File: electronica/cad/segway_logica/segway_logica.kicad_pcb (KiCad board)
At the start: 2 copper layers, 100 x 82 mm, 17 parts, among them J20 Cable lógica-potencia 2x8, J4 Paro MPT0,5 1=GND 2=PARO (NC), J7 Encoder IZQ PT1,5 1=V 2=A 3=B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, J8 Encoder DER PT1,5 1=GND 2=A 3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

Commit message: electronica: PCB v0.1 de la placa de potencia, una cara, DRC limpio (ELE-032)
- Placa de potencia 150 x 110 mm: barra VM_BUS, lomo GND en estrella entre los
  pads de los fusibles, ramas por canal de motor, franja de servos y banda
  lógica. DRC 0 errores, 0 sin conectar, 0 de paridad; 7 puentes fijos.
- Ruteo híbrido (TEC-05): esqueleto y bus I2C a mano (J20 -> A7 -> A5 ->
  corredor bajo los módulos -> A6), Freerouting solo para nets simples, vías
  prohibidas sobre componentes y poda automática de puentes redundantes.
- Cable J20 y GPIO reordenados por geometría (VBAT en GPIO3, ALERT en GPIO8,
  columna par servos/IN); placa de lógica regenerada y re-verificada (0/0/0).
- J20.11 sin conexión en la potencia; INA226 sin separador opcional.
- Supuestos SUP-04/15/24/28/72 actualizados y SUP-75 a SUP-77 nuevos.

Co-Authored-By: Claude Opus 5.5 <noreply@anthropic.com>
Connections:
- A1 pad 12: /VBAT_ADC -> /INA_ALERT
- A1 pad 13: /INA_ALERT -> /VBAT_ADC
- A1 pad 15: /IN1_DER_MCU -> /SERVO_IZQ_MCU
- A1 pad 16: /IN2_DER_MCU -> /SERVO_DER_MCU
- A1 pad 17: /IN1_IZQ_MCU -> /IN2_DER_MCU
- A1 pad 18: /IN2_IZQ_MCU -> /IN1_DER_MCU
- A1 pad 19: /SERVO_IZQ_MCU -> /IN2_IZQ_MCU
- A1 pad 20: /SERVO_DER_MCU -> /IN1_IZQ_MCU
- J20 pad 1: /INA_ALERT -> /VBAT_ADC
- J20 pad 10: /SERVO_IZQ_MCU -> /IN2_IZQ_MCU
- J20 pad 12: /SERVO_DER_MCU -> /IN1_IZQ_MCU
- J20 pad 2: /IN1_DER_MCU -> /SERVO_IZQ_MCU
- J20 pad 3: /VBAT_ADC -> /INA_ALERT
- J20 pad 4: /IN2_DER_MCU -> /SERVO_DER_MCU
- J20 pad 6: /IN1_IZQ_MCU -> /IN2_DER_MCU
- J20 pad 8: /IN2_IZQ_MCU -> /IN1_DER_MCU
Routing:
- net /INA_ALERT: track 15.2 -> 25.4 mm
- net /VBAT_ADC: track 25.4 -> 15.2 mm

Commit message: electronica: expansión de la placa de lógica, tiras hembra junto a la ESP32-S3 (ELE-037)
Pedido del equipo: pines hembra en paralelo a la controladora para sumar
sensores (ultrasonido, infrarrojo).

- J24 y J25: tiras hembra 1x22 pegadas a cada hilera de A1, pin a pin.
  Huellas propias con el courtyard recortado del lado de A1.
- J26: tira hembra 1x6 de alimentación (GND, 3V3, 5V_MCU).
- J20.11 sin conexión también en la lógica; rótulos de cobre bajados
  para que el relleno GND no quede partido.
- generar_esquema.py: altura correcta de los conectores de una hilera
  (antes se pisaban las etiquetas y el comparador detectaba cortos).
- ERC 0, netlist coincidente, DRC 0 errores / 0 sin conectar / 0 paridad.
- SUP-72 y SUP-77 cambiados; SUP-78 y SUP-79 nuevos.

Co-Authored-By: Claude Opus 5.5 <noreply@anthropic.com>
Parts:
- added J24: Expansión ESP32 IZQ (A1.1-22), segway_modulos:Zocalo_expansion_izq_1x22_P2.54mm, F.Cu at (91.4, 41.9)
- added J25: Expansión ESP32 DER (A1.23-44), segway_modulos:Zocalo_expansion_der_1x22_P2.54mm, F.Cu at (121.9, 41.9)
- added J26: Alim. sensores 1-2 GND 3-4 3V3 5-6 5V, Connector_PinSocket_2.54mm:PinSocket_1x06_P2.54mm_Vertical, F.Cu at (63.5, 91.4)
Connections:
- A1 pad 14: unconnected-(A1-GPIO46-Pad14) -> /GPIO46
- A1 pad 24: unconnected-(A1-GPIO43/TX-Pad24) -> /GPIO43
- A1 pad 25: unconnected-(A1-GPIO44/RX-Pad25) -> /GPIO44
- A1 pad 26: unconnected-(A1-GPIO1-Pad26) -> /GPIO1
- A1 pad 27: unconnected-(A1-GPIO2-Pad27) -> /GPIO2
- A1 pad 28: unconnected-(A1-GPIO42-Pad28) -> /GPIO42
- A1 pad 29: unconnected-(A1-GPIO41-Pad29) -> /GPIO41
- A1 pad 3: unconnected-(A1-RST-Pad3) -> /RST
- A1 pad 30: unconnected-(A1-GPIO40-Pad30) -> /GPIO40
- A1 pad 31: unconnected-(A1-GPIO39-Pad31) -> /GPIO39
- A1 pad 32: unconnected-(A1-GPIO38-Pad32) -> /GPIO38
- A1 pad 33: unconnected-(A1-GPIO37-Pad33) -> /GPIO37
- A1 pad 34: unconnected-(A1-GPIO36-Pad34) -> /GPIO36
- A1 pad 35: unconnected-(A1-GPIO35-Pad35) -> /GPIO35
- A1 pad 36: unconnected-(A1-GPIO0-Pad36) -> /GPIO0
- A1 pad 37: unconnected-(A1-GPIO45-Pad37) -> /GPIO45
- A1 pad 38: unconnected-(A1-GPIO48-Pad38) -> /GPIO48
- A1 pad 39: unconnected-(A1-GPIO47-Pad39) -> /GPIO47
- A1 pad 40: unconnected-(A1-GPIO21-Pad40) -> /GPIO21
- A1 pad 41: unconnected-(A1-GPIO20-Pad41) -> /GPIO20
- A1 pad 42: unconnected-(A1-GPIO19-Pad42) -> /GPIO19
- J20 pad 11: /GND -> unconnected-(J20-Pin_11-Pad11)
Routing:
- net /5V_MCU: track 10.2 -> 20.8 mm
- net /3V3_MCU: track 168.1 -> 177.0 mm
- net /GND: track 34.9 -> 43.5 mm
- net /GPIO48: track 0.00 -> 2.54 mm
- net /GPIO47: track 0.00 -> 2.54 mm
- net /GPIO45: track 0.00 -> 2.54 mm
- net /GPIO44: track 0.00 -> 2.54 mm
- net /GPIO43: track 0.00 -> 2.54 mm
- net /GPIO42: track 0.00 -> 2.54 mm
- net /GPIO41: track 0.00 -> 2.54 mm
- net /GPIO40: track 0.00 -> 2.54 mm
- net /GPIO39: track 0.00 -> 2.54 mm
- net /GPIO38: track 0.00 -> 2.54 mm
- net /GPIO37: track 0.00 -> 2.54 mm
- net /GPIO36: track 0.00 -> 2.54 mm
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
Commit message: electronica: rótulos de cobre, revisión independiente y control eléctrico (ELE-039)
- Rótulos de polaridad y de fusibles en el cobre de las dos placas,
  ubicados con ubicar_rotulos.py sin partir el relleno GND (SUP-14).
- Revisión independiente del conexionado contra las fichas: módulos,
  cable, polaridades y niveles correctos. Riesgos nuevos: A7 y A8 entran
  girados y queman (SUP-80), aleta de Q1 con tensión (SUP-20), I2C junto
  a PWM en el cable (SUP-81).
- auditoria_electrica.py: control repetible del sistema (cable, pines
  críticos, 5 V lejos de la ESP32, módulos girados, I2C, cuellos de
  pista, niveles). Informe: 0 fallas, 6 avisos.
- J26 reordenado con GND en el medio; textos de la Blue Pill en la
  especificación corregidos.
- ERC 0 y netlist coincidente; DRC 0/0/0 en las dos placas; salidas de
  fabricación regeneradas.

Co-Authored-By: Claude Opus 5.5 <noreply@anthropic.com>
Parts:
- J26: value Alim. sensores 1-2 GND 3-4 3V3 5-6 5V -> Alim. sensores 1-2 3V3 3-4 GND 5-6 5V
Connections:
- J26 pad 1: /GND -> /3V3_MCU
- J26 pad 2: /GND -> /3V3_MCU
- J26 pad 3: /3V3_MCU -> /GND
- J26 pad 4: /3V3_MCU -> /GND
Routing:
- net /GND: track 43.5 -> 38.1 mm
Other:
- board text added: "1"
- board text added: "ENC IZQ"
- board text added: "G"

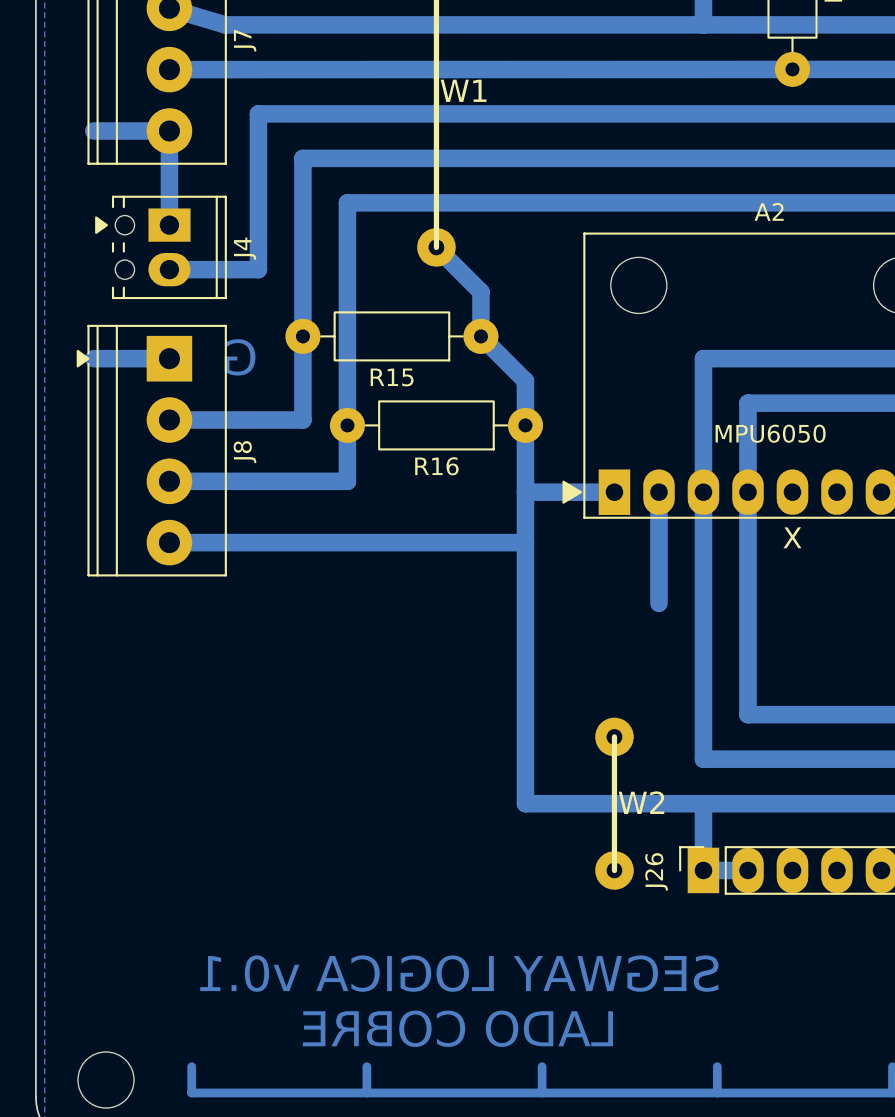
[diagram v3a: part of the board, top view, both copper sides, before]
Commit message: electronica: PCB v0.2 de las dos placas, auditada (ELE-040)
- J3 y J4 pasan a pads para soldar el cable del interruptor y del paro.
- Montaje: A1-A4 en zócalo, A5-A8 soldados (DEC-20). A1 codificada:
  pin 24 cortado y posición tapada (revisión independiente: entraba
  girada o corrida y se quemaba).
- auditoria_electrica.py prueba giros y corrimientos de los módulos
  enchufados; 0 fallas, 3 avisos.
- Rótulos ambiguos de fusibles y VCC quitados; continuidad del cable
  J20 antes de enchufar; precinto en J3.
- Documentación v0.2, lista de compras, fabricación en rev-0.2.
- ERC 0, netlist coincidente, DRC 0/0/0 en las dos placas.

Co-Authored-By: Claude Opus 5.5 <noreply@anthropic.com>
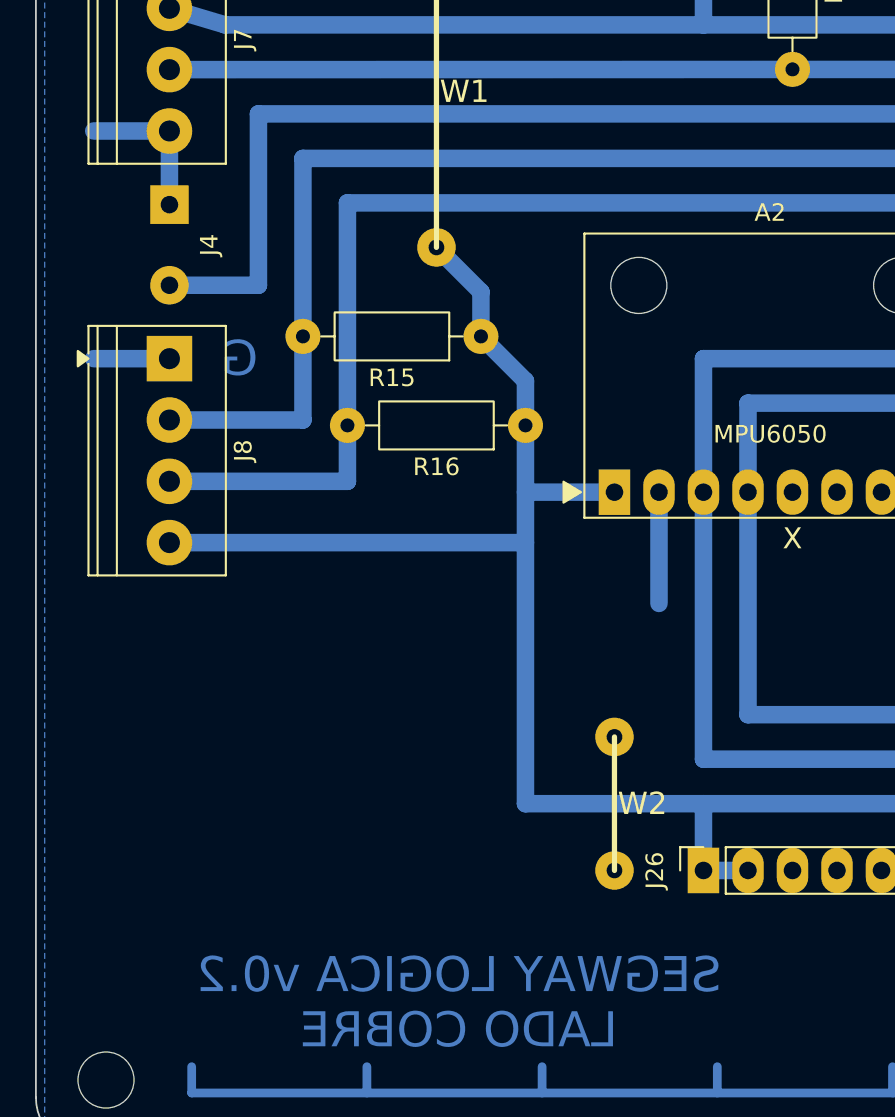
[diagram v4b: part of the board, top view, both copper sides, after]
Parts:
- J4: value Paro MPT0,5 1=GND 2=PARO (NC) -> Paro NC 1=GND 2=PARO, cable soldado; footprint TerminalBlock_Phoenix:TerminalBlock_Phoenix_MPT-0,5-2-2.54_1x02_P2.54mm_Horizontal -> Connector_Wire:SolderWire-0.5sqmm_1x02_P4.6mm_D0.9mm_OD2.1mm
- moved J4 1.17 mm to (33.0, 53.4)
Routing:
- net /GND: track 38.1 -> 37.0 mm
- net /PARO_CONT: track 72.5 -> 73.4 mm
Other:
- board text added: "SEGWAY LOGICA v0.2"
- board text removed: "SEGWAY LOGICA v0.1"
